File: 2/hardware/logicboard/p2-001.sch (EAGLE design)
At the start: 66 parts, among them IC1 74LS06N, IC101 74LS153D, IC102 LTC485S, IC103 LTC485S, IC2 4066N, J1 MKR, J101 Qwiic, J102 Qwiic, J103 Qwiic, J104 Qwiic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

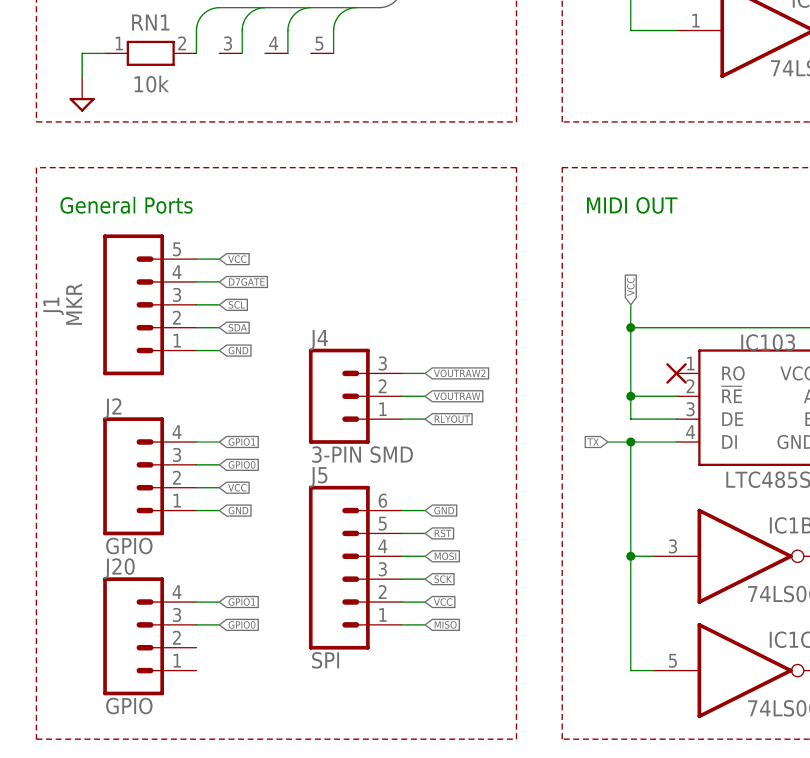
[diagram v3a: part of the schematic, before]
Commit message: Extra I2C conn.
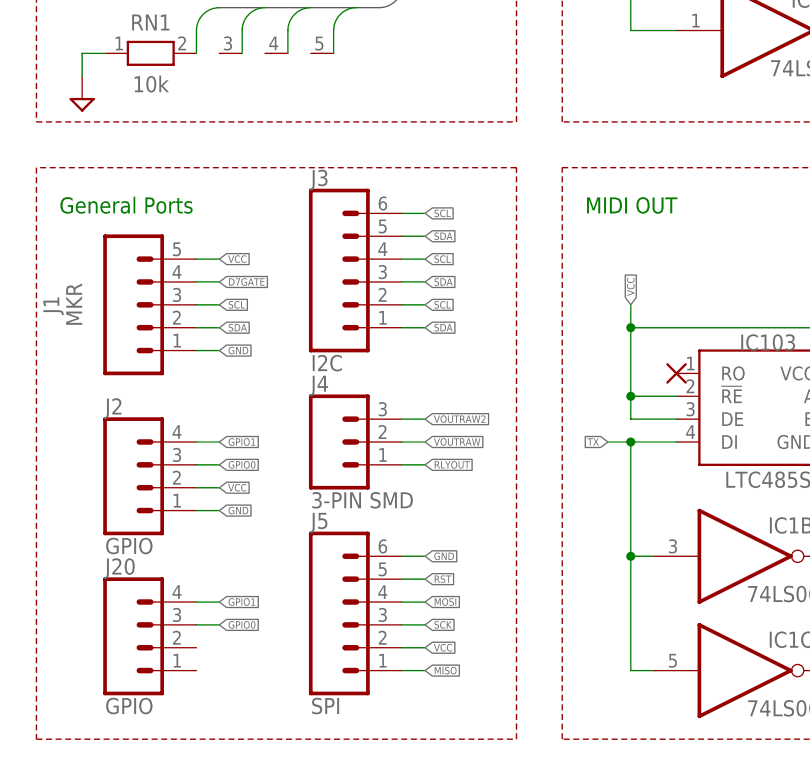
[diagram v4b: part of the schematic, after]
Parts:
- added J3: I2C, SparkFun-Connectors:CONN_061.27MM
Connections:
- net SCL: now also J3.2, J3.4, J3.6
- net SDA: now also J3.1, J3.3, J3.5
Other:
- moved on the sheet: J4, J5
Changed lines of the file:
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@@
 <part name="J20" library="SparkFun-Connectors" library_urn="urn:adsk.eagle:library:513" deviceset="CONN_04" device="1.27MM" package3d_urn="urn:adsk.eagle:package:38086/1" value="GPIO"/>
 <part name="JP4" library="pinhead" library_urn="urn:adsk.eagle:library:325" deviceset="PINHD-1X4" device="" package3d_urn="urn:adsk.eagle:package:22407/2" value="LEDSW"/>
+<part name="J3" library="SparkFun-Connectors" library_urn="urn:adsk.eagle:library:513" deviceset="CONN_06" device="1.27MM" package3d_urn="urn:adsk.eagle:package:38131/1" value="I2C"/>
 </parts>
 <sheets>
@@
 <attribute name="VALUE" x="153.797" y="207.518" size="1.778" layer="96"/>
 </instance>
-<instance part="J4" gate="J$1" x="88.9" y="45.72" smashed="yes">
-<attribute name="VALUE" x="86.36" y="38.354" size="1.778" layer="96" font="vector"/>
-<attribute name="NAME" x="86.36" y="51.308" size="1.778" layer="95" font="vector"/>
-</instance>
-<instance part="J5" gate="G$1" x="91.44" y="25.4" smashed="yes">
-<attribute name="VALUE" x="86.36" y="15.494" size="1.778" layer="96" font="vector"/>
-<attribute name="NAME" x="86.36" y="36.068" size="1.778" layer="95" font="vector"/>
+<instance part="J4" gate="J$1" x="88.9" y="40.64" smashed="yes">
+<attribute name="VALUE" x="86.36" y="33.274" size="1.778" layer="96" font="vector"/>
+<attribute name="NAME" x="86.36" y="46.228" size="1.778" layer="95" font="vector"/>
+</instance>
+<instance part="J5" gate="G$1" x="91.44" y="20.32" smashed="yes">
+<attribute name="VALUE" x="86.36" y="10.414" size="1.778" layer="96" font="vector"/>
+<attribute name="NAME" x="86.36" y="30.988" size="1.778" layer="95" font="vector"/>
 </instance>
 <instance part="J2" gate="G$1" x="68.58" y="35.56" smashed="yes">
@@
 <attribute name="NAME" x="36.83" y="170.815" size="1.778" layer="95" rot="MR0"/>
 <attribute name="VALUE" x="36.83" y="154.94" size="1.778" layer="96" rot="MR0"/>
+</instance>
+<instance part="J3" gate="G$1" x="91.44" y="58.42" smashed="yes">
+<attribute name="VALUE" x="86.36" y="48.514" size="1.778" layer="96" font="vector"/>
+<attribute name="NAME" x="86.36" y="69.088" size="1.778" layer="95" font="vector"/>
 </instance>
 </instances>
@@
 <segment>
 <pinref part="J5" gate="G$1" pin="6"/>
-<wire x1="96.52" y1="33.02" x2="99.06" y2="33.02" width="0.1524" layer="91"/>
-<label x="99.06" y="33.02" size="0.8128" layer="95" xref="yes"/>
+<wire x1="96.52" y1="27.94" x2="99.06" y2="27.94" width="0.1524" layer="91"/>
+<label x="99.06" y="27.94" size="0.8128" layer="95" xref="yes"/>
 </segment>
 <segment>
@@
 </segment>
 <segment>
-<wire x1="96.52" y1="22.86" x2="99.06" y2="22.86" width="0.1524" layer="91"/>
-<label x="99.06" y="22.86" size="0.8128" layer="95" xref="yes"/>
+<wire x1="96.52" y1="17.78" x2="99.06" y2="17.78" width="0.1524" layer="91"/>
+<label x="99.06" y="17.78" size="0.8128" layer="95" xref="yes"/>
 <pinref part="J5" gate="G$1" pin="2"/>
 </segment>
@@
 </segment>
 <segment>
-<wire x1="96.52" y1="30.48" x2="99.06" y2="30.48" width="0.1524" layer="91"/>
-<label x="99.06" y="30.48" size="0.8128" layer="95" xref="yes"/>
+<wire x1="96.52" y1="25.4" x2="99.06" y2="25.4" width="0.1524" layer="91"/>
+<label x="99.06" y="25.4" size="0.8128" layer="95" xref="yes"/>
 <pinref part="J5" gate="G$1" pin="5"/>
 </segment>
@@
 <label x="241.3" y="147.32" size="0.8128" layer="95" xref="yes"/>
 </segment>
+<segment>
+<pinref part="J3" gate="G$1" pin="1"/>
+<wire x1="96.52" y1="53.34" x2="99.06" y2="53.34" width="0.1524" layer="91"/>
+<label x="99.06" y="53.34" size="0.8128" layer="95" xref="yes"/>
+</segment>
+<segment>
+<pinref part="J3" gate="G$1" pin="3"/>
+<wire x1="96.52" y1="58.42" x2="99.06" y2="58.42" width="0.1524" layer="91"/>
+<label x="99.06" y="58.42" size="0.8128" layer="95" xref="yes"/>
+</segment>
+<segment>
+<pinref part="J3" gate="G$1" pin="5"/>
+<wire x1="96.52" y1="63.5" x2="99.06" y2="63.5" width="0.1524" layer="91"/>
+<label x="99.06" y="63.5" size="0.8128" layer="95" xref="yes"/>
+</segment>
 </net>
 <net name="SCL" class="0">
@@
 <wire x1="238.76" y1="142.24" x2="241.3" y2="142.24" width="0.1524" layer="91"/>
 <label x="241.3" y="142.24" size="0.8128" layer="95" xref="yes"/>
+</segment>
+<segment>
+<pinref part="J3" gate="G$1" pin="2"/>
+<wire x1="96.52" y1="55.88" x2="99.06" y2="55.88" width="0.1524" layer="91"/>
+<label x="99.06" y="55.88" size="0.8128" layer="95" xref="yes"/>
+</segment>
+<segment>
+<pinref part="J3" gate="G$1" pin="4"/>
+<wire x1="96.52" y1="60.96" x2="99.06" y2="60.96" width="0.1524" layer="91"/>
+<label x="99.06" y="60.96" size="0.8128" layer="95" xref="yes"/>
+</segment>
+<segment>
+<pinref part="J3" gate="G$1" pin="6"/>
+<wire x1="96.52" y1="66.04" x2="99.06" y2="66.04" width="0.1524" layer="91"/>
+<label x="99.06" y="66.04" size="0.8128" layer="95" xref="yes"/>
 </segment>
 </net>
@@
 <segment>
 <pinref part="J4" gate="J$1" pin="3"/>
-<wire x1="96.52" y1="48.26" x2="99.06" y2="48.26" width="0.1524" layer="91"/>
-<label x="99.06" y="48.26" size="0.8128" layer="95" xref="yes"/>
+<wire x1="96.52" y1="43.18" x2="99.06" y2="43.18" width="0.1524" layer="91"/>
+<label x="99.06" y="43.18" size="0.8128" layer="95" xref="yes"/>
 </segment>
 </net>
@@
 </segment>
 <segment>
-<wire x1="96.52" y1="45.72" x2="99.06" y2="45.72" width="0.1524" layer="91"/>
-<label x="99.06" y="45.72" size="0.8128" layer="95" xref="yes"/>
+<wire x1="96.52" y1="40.64" x2="99.06" y2="40.64" width="0.1524" layer="91"/>
+<label x="99.06" y="40.64" size="0.8128" layer="95" xref="yes"/>
 <pinref part="J4" gate="J$1" pin="2"/>
 </segment>
@@
 </segment>
 <segment>
-<wire x1="96.52" y1="43.18" x2="99.06" y2="43.18" width="0.1524" layer="91"/>
-<label x="99.06" y="43.18" size="0.8128" layer="95" xref="yes"/>
+<wire x1="96.52" y1="38.1" x2="99.06" y2="38.1" width="0.1524" layer="91"/>
+<label x="99.06" y="38.1" size="0.8128" layer="95" xref="yes"/>
 <pinref part="J4" gate="J$1" pin="1"/>
 </segment>
@@
 </segment>
 <segment>
-<wire x1="96.52" y1="20.32" x2="99.06" y2="20.32" width="0.1524" layer="91"/>
-<label x="99.06" y="20.32" size="0.8128" layer="95" xref="yes"/>
+<wire x1="96.52" y1="15.24" x2="99.06" y2="15.24" width="0.1524" layer="91"/>
+<label x="99.06" y="15.24" size="0.8128" layer="95" xref="yes"/>
 <pinref part="J5" gate="G$1" pin="1"/>
 </segment>
@@
 </segment>
 <segment>
-<wire x1="96.52" y1="25.4" x2="99.06" y2="25.4" width="0.1524" layer="91"/>
-<label x="99.06" y="25.4" size="0.8128" layer="95" xref="yes"/>
+<wire x1="96.52" y1="20.32" x2="99.06" y2="20.32" width="0.1524" layer="91"/>
+<label x="99.06" y="20.32" size="0.8128" layer="95" xref="yes"/>
 <pinref part="J5" gate="G$1" pin="3"/>
 </segment>
@@
 </segment>
 <segment>
-<wire x1="96.52" y1="27.94" x2="99.06" y2="27.94" width="0.1524" layer="91"/>
-<label x="99.06" y="27.94" size="0.8128" layer="95" xref="yes"/>
+<wire x1="96.52" y1="22.86" x2="99.06" y2="22.86" width="0.1524" layer="91"/>
+<label x="99.06" y="22.86" size="0.8128" layer="95" xref="yes"/>
 <pinref part="J5" gate="G$1" pin="4"/>
 </segment>
